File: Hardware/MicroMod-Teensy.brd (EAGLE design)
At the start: 22 x 22.8 mm, 76 parts, among them J1 MICROMOD-2222, Q1 20V/4.2A/52mΩ/1.4W, Q2 20V/0.2A/8MHz/1.2Ω/1Vth, U1 IMXRT1062DV10X10, U2 W25QXX3X2, U3 MKL02Z32VFG4, Y1 32.768kHz, Y2 24MHz

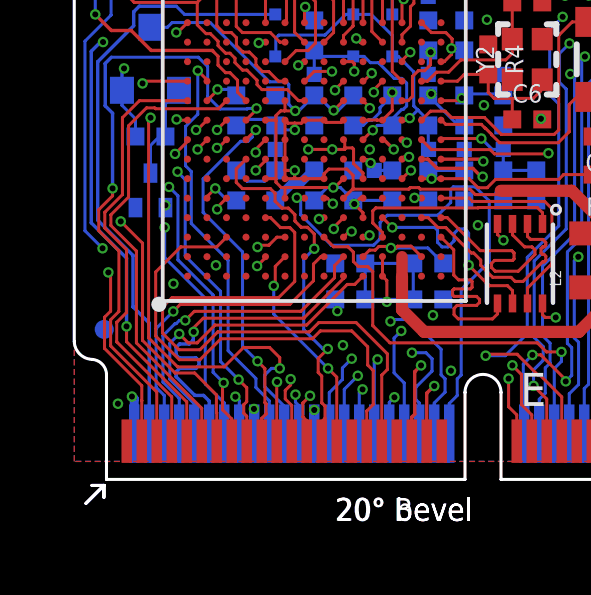
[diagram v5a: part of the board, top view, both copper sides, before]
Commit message: Add ordering instructions
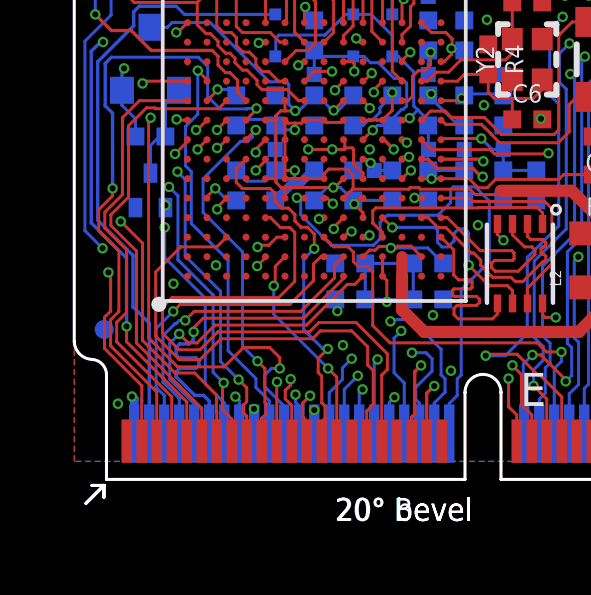
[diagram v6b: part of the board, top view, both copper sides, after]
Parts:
- added LOGO3: SPECIAL_INSTRUCTIONS-ORDERING, SparkFun-Aesthetics:ORDERING_INSTRUCTIONS
- moved LOGO2 24.2 mm to (11.4, -21.6)
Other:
- board text added: "0.8mm PCB 45 degree chamfered edge Four layer design"
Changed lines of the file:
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@@
 <?xml version="1.0" encoding="utf-8"?>
 <!DOCTYPE eagle SYSTEM "eagle.dtd">
-<eagle version="9.5.2">
+<eagle version="9.6.0">
 <drawing>
 <settings>
@@
 <setting verticaltext="up"/>
 </settings>
-<grid distance="1" unitdist="mm" unit="mm" style="lines" multiple="1" display="yes" altdistance="0.05" altunitdist="mm" altunit="mm"/>
+<grid distance="0.05" unitdist="inch" unit="inch" style="lines" multiple="1" display="yes" altdistance="0.005" altunitdist="inch" altunit="inch"/>
 <layers>
 <layer number="1" name="Top" color="4" fill="1" visible="yes" active="yes"/>
-<layer number="2" name="Horz" color="1" fill="3" visible="no" active="yes"/>
-<layer number="15" name="Vert" color="4" fill="6" visible="no" active="yes"/>
+<layer number="2" name="Horz" color="1" fill="3" visible="yes" active="yes"/>
+<layer number="15" name="Vert" color="4" fill="6" visible="yes" active="yes"/>
 <layer number="16" name="Bottom" color="1" fill="1" visible="yes" active="yes"/>
 <layer number="17" name="Pads" color="2" fill="1" visible="yes" active="yes"/>
@@
 <layer number="23" name="tOrigins" color="15" fill="1" visible="yes" active="yes"/>
 <layer number="24" name="bOrigins" color="15" fill="1" visible="yes" active="yes"/>
-<layer number="25" name="tNames" color="7" fill="1" visible="no" active="yes"/>
-<layer number="26" name="bNames" color="7" fill="1" visible="no" active="yes"/>
-<layer number="27" name="tValues" color="7" fill="1" visible="no" active="yes"/>
-<layer number="28" name="bValues" color="7" fill="1" visible="no" active="yes"/>
-<layer number="29" name="tStop" color="7" fill="3" visible="no" active="yes"/>
-<layer number="30" name="bStop" color="7" fill="6" visible="no" active="yes"/>
-<layer number="31" name="tCream" color="7" fill="4" visible="no" active="yes"/>
-<layer number="32" name="bCream" color="7" fill="5" visible="no" active="yes"/>
-<layer number="33" name="tFinish" color="6" fill="3" visible="no" active="yes"/>
-<layer number="34" name="bFinish" color="6" fill="6" visible="no" active="yes"/>
-<layer number="35" name="tGlue" color="7" fill="4" visible="no" active="yes"/>
-<layer number="36" name="bGlue" color="7" fill="5" visible="no" active="yes"/>
-<layer number="37" name="tTest" color="7" fill="1" visible="no" active="yes"/>
-<layer number="38" name="bTest" color="7" fill="1" visible="no" active="yes"/>
-<layer number="39" name="tKeepout" color="4" fill="11" visible="no" active="yes"/>
-<layer number="40" name="bKeepout" color="1" fill="11" visible="no" active="yes"/>
-<layer number="41" name="tRestrict" color="4" fill="10" visible="no" active="yes"/>
-<layer number="42" name="bRestrict" color="1" fill="10" visible="no" active="yes"/>
-<layer number="43" name="vRestrict" color="2" fill="10" visible="no" active="yes"/>
-<layer number="44" name="Drills" color="7" fill="1" visible="no" active="yes"/>
+<layer number="25" name="tNames" color="7" fill="1" visible="yes" active="yes"/>
+<layer number="26" name="bNames" color="7" fill="1" visible="yes" active="yes"/>
+<layer number="27" name="tValues" color="7" fill="1" visible="yes" active="yes"/>
+<layer number="28" name="bValues" color="7" fill="1" visible="yes" active="yes"/>
+<layer number="29" name="tStop" color="7" fill="3" visible="yes" active="yes"/>
+<layer number="30" name="bStop" color="7" fill="6" visible="yes" active="yes"/>
+<layer number="31" name="tCream" color="7" fill="4" visible="yes" active="yes"/>
+<layer number="32" name="bCream" color="7" fill="5" visible="yes" active="yes"/>
+<layer number="33" name="tFinish" color="6" fill="3" visible="yes" active="yes"/>
+<layer number="34" name="bFinish" color="6" fill="6" visible="yes" active="yes"/>
+<layer number="35" name="tGlue" color="7" fill="4" visible="yes" active="yes"/>
+<layer number="36" name="bGlue" color="7" fill="5" visible="yes" active="yes"/>
+<layer number="37" name="tTest" color="7" fill="1" visible="yes" active="yes"/>
+<layer number="38" name="bTest" color="7" fill="1" visible="yes" active="yes"/>
+<layer number="39" name="tKeepout" color="4" fill="11" visible="yes" active="yes"/>
+<layer number="40" name="bKeepout" color="1" fill="11" visible="yes" active="yes"/>
+<layer number="41" name="tRestrict" color="4" fill="10" visible="yes" active="yes"/>
+<layer number="42" name="bRestrict" color="1" fill="10" visible="yes" active="yes"/>
+<layer number="43" name="vRestrict" color="2" fill="10" visible="yes" active="yes"/>
+<layer number="44" name="Drills" color="7" fill="1" visible="yes" active="yes"/>
 <layer number="45" name="Holes" color="7" fill="1" visible="yes" active="yes"/>
-<layer number="46" name="Milling" color="3" fill="1" visible="no" active="yes"/>
-<layer number="47" name="Measures" color="7" fill="1" visible="no" active="yes"/>
-<layer number="48" name="Document" color="7" fill="1" visible="no" active="yes"/>
+<layer number="46" name="Milling" color="3" fill="1" visible="yes" active="yes"/>
+<layer number="47" name="Measures" color="7" fill="1" visible="yes" active="yes"/>
+<layer number="48" name="Document" color="7" fill="1" visible="yes" active="yes"/>
 <layer number="49" name="Reference" color="7" fill="1" visible="yes" active="yes"/>
-<layer number="50" name="dxf" color="7" fill="1" visible="no" active="yes"/>
+<layer number="50" name="dxf" color="7" fill="1" visible="yes" active="yes"/>
 <layer number="51" name="tDocu" color="6" fill="1" visible="yes" active="yes"/>
-<layer number="52" name="bDocu" color="7" fill="1" visible="no" active="yes"/>
+<layer number="52" name="bDocu" color="7" fill="1" visible="yes" active="yes"/>
 <layer number="91" name="Nets" color="2" fill="1" visible="no" active="no"/>
 <layer number="92" name="Busses" color="1" fill="1" visible="no" active="no"/>
@@
 <wire x1="-0.86" y1="19" x2="-0.86" y2="5" width="0.1016" layer="51"/>
 <text x="19.94" y="6" size="0.75" layer="16" font="vector" ratio="20" rot="MR0" align="center">v11</text>
+<text x="29.53" y="31.67" size="1.778" layer="51" font="vector" ratio="15">0.8mm PCB
+45 degree chamfered edge
+Four layer design</text>
 </plain>
 <attributes>
@@
 <attribute name="VALUE" x="1.68" y="11.992" size="0.6096" layer="28" font="vector" ratio="20" rot="MR180" align="top-center"/>
 </element>
-<element name="LOGO2" library="SparkFun-Aesthetics" package="DUMMY" value="OSHW-LOGONO_SILK" x="-12.7" y="-22.86" smashed="yes"/>
+<element name="LOGO2" library="SparkFun-Aesthetics" package="DUMMY" value="OSHW-LOGONO_SILK" x="11.43" y="-21.59" smashed="yes"/>
+<element name="LOGO3" library="SparkFun-Aesthetics" package="ORDERING_INSTRUCTIONS" value="SPECIAL_INSTRUCTIONS-ORDERING" x="26.67" y="50.8" smashed="yes"/>
 </elements>
 <signals>
@@
 <wire x1="1.12125" y1="15.12125" x2="-0.07775" y2="13.92225" width="0.1143" layer="16"/>
 <wire x1="-0.07775" y1="8.6426125" x2="1.0995" y2="7.4653625" width="0.1143" layer="16"/>
-<wire x1="1.0995" y1="5.7505" x2="1.1" y2="5.75" width="0.1143" layer="16"/>
 <wire x1="1.0995" y1="7.4653625" x2="1.0995" y2="5.7505" width="0.1143" layer="16"/>
 <wire x1="1.12125" y1="15.58575625" x2="1.12125" y2="15.12125" width="0.1143" layer="16"/>
 <wire x1="-0.07775" y1="13.92225" x2="-0.07775" y2="8.6426125" width="0.1143" layer="16"/>
 <wire x1="1.64" y1="1.525" x2="1.64" y2="5.21" width="0.1143" layer="16"/>
-<wire x1="1.64" y1="5.21" x2="1.1" y2="5.75" width="0.1143" layer="16"/>
+<wire x1="1.64" y1="5.21" x2="1.0995" y2="5.7505" width="0.1143" layer="16"/>
 </signal>
 <signal name="PROGRAM">
@@
 <wire x1="14.50485" y1="4.82446875" x2="14.50485" y2="9.65433125" width="0.1143" layer="15"/>
 <wire x1="14.50485" y1="9.65433125" x2="13.70485" y2="10.45433125" width="0.1143" layer="15"/>
-<wire x1="13.70485" y1="10.45433125" x2="13.70485" y2="11" width="0.1143" layer="15"/>
-<wire x1="13.70485" y1="11" x2="13.70485" y2="11.25" width="0.1143" layer="15"/>
 <wire x1="11.47074375" y1="19.38495" x2="11.19325625" y2="19.38495" width="0.1143" layer="15"/>
 <wire x1="11.19325625" y1="19.38495" x2="11.18619375" y2="19.3778875" width="0.1143" layer="15"/>
 <wire x1="11.18619375" y1="19.3778875" x2="10.9721125" y2="19.3778875" width="0.1143" layer="15"/>
-<wire x1="13.70485" y1="11.25" x2="13.70485" y2="17.15084375" width="0.1143" layer="15"/>
+<wire x1="13.70485" y1="10.45433125" x2="13.70485" y2="17.15084375" width="0.1143" layer="15"/>
 <wire x1="13.70485" y1="17.15084375" x2="11.47074375" y2="19.38495" width="0.1143" layer="15"/>
 </signal>
@@
 </drawing>
 <compatibility>
+<note version="6.3" minversion="6.2.2" severity="warning">
+Since Version 6.2.2 text objects can contain more than one line,
+which will not be processed correctly with this version.
+</note>
 <note version="8.3" severity="warning">
 Since Version 8.3, EAGLE supports URNs for individual library

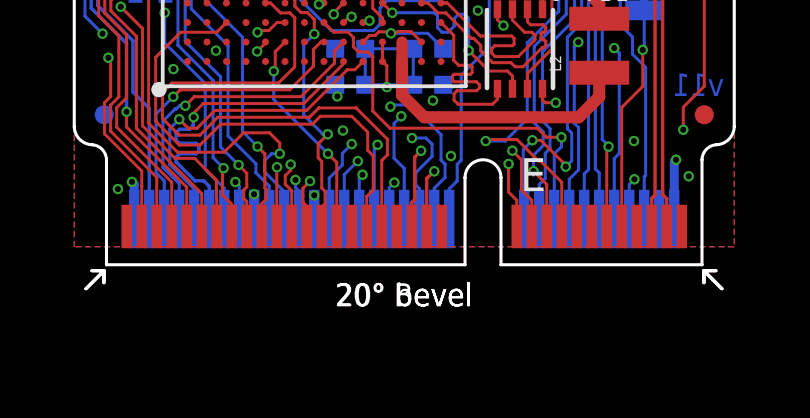
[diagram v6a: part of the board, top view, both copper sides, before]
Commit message: Update Micromod connector to current version
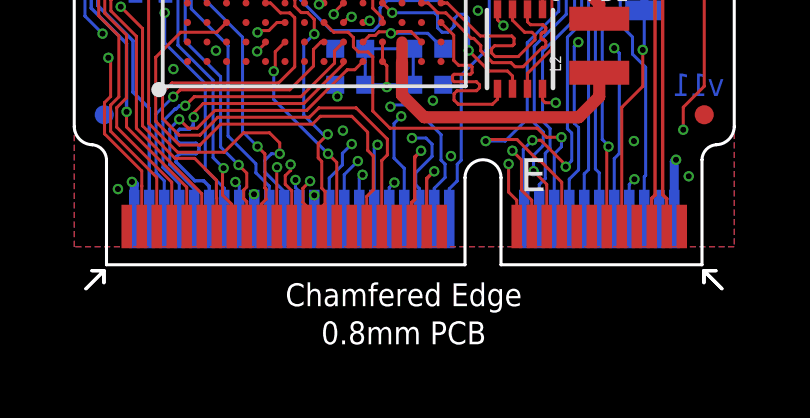
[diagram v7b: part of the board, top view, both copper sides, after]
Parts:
- J1: device Teensy:M.2-CARD-E-22 -> SparkFun-MicroMod:M.2-CARD-E-22
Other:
- board text removed: "20° bevel"
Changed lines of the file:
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@@
 <wire x1="0.215" y1="0" x2="0.215" y2="3.5" width="0.1016" layer="20"/>
 <wire x1="20.065" y1="3.5" x2="20.065" y2="0" width="0.1016" layer="20"/>
-<text x="10.14" y="-1" size="0.762" layer="46" rot="R180" align="center">20° bevel</text>
 <wire x1="20.54" y1="4" x2="20.065" y2="3.5" width="0.1016" layer="20" curve="84.949116"/>
 <wire x1="-0.26" y1="4" x2="0.215" y2="3.5" width="0.1016" layer="20" curve="-83.820277"/>
@@
 <element name="U$5" library="buzzard_labels (1)" package="MICROMOD0" value="" x="20.74" y="15.5" smashed="yes" rot="MR0"/>
 <element name="U$7" library="SparkFun-Buzzard" package="MEAS_32" value="" x="20.24" y="6.6" smashed="yes" rot="MR90"/>
-<element name="J1" library="Teensy" package="M.2-CARD-E-22" value="MICROMOD-2222" x="10.14" y="0" smashed="yes"/>
+<element name="J1" library="SparkFun-MicroMod" package="M.2-CARD-E-22" value="MICROMOD-2222" x="10.14" y="0" smashed="yes"/>
 <element name="TP2" library="SparkFun-Connectors" package="PAD.02X.02" value="" x="9.14" y="10.3" smashed="yes" rot="MR0"/>
 <element name="Q1" library="SparkFun-DiscreteSemi" package="SOT23-3" value="20V/4.2A/52mΩ/1.4W" x="1.68" y="13.97" smashed="yes" rot="MR0">
@@
 <wire x1="7.0984" y1="10.3" x2="7.14" y2="10.3" width="0.3048" layer="16"/>
 <wire x1="6.6682" y1="9.8698" x2="7.0984" y2="10.3" width="0.3048" layer="16"/>
+<wire x1="14.14" y1="22" x2="18.263" y2="21" width="0" layer="19" extent="1-1"/>
+<wire x1="14.14" y1="19" x2="14.14" y2="22" width="0" layer="19" extent="16-16"/>
+<wire x1="14.74" y1="15.9" x2="14.14" y2="18.17145" width="0" layer="19" extent="1-16"/>
+<wire x1="15.496" y1="16.123" x2="14.74" y2="15.9" width="0" layer="19" extent="1-1"/>
+<wire x1="12.896" y1="15.323" x2="14.74" y2="15.9" width="0" layer="19" extent="1-1"/>
+<wire x1="12.14" y1="15.3" x2="12.896" y2="15.323" width="0" layer="19" extent="16-16"/>
+<wire x1="11.365" y1="15.225" x2="12.14" y2="15.3" width="0" layer="19" extent="1-16"/>
+<wire x1="10.94" y1="15.3" x2="11.365" y2="15.225" width="0" layer="19" extent="1-16"/>
+<wire x1="12.94" y1="14.5" x2="12.896" y2="15.323" width="0" layer="19" extent="1-1"/>
+<wire x1="12.196" y1="16.223" x2="12.14" y2="15.3" width="0" layer="19" extent="16-16"/>
+<wire x1="12.796" y1="12.473" x2="12.94" y2="14.5" width="0" layer="19" extent="1-1"/>
+<wire x1="13.44" y1="11.8" x2="12.796" y2="12.473" width="0" layer="19" extent="16-16"/>
+<wire x1="12.14" y1="11.8" x2="12.796" y2="12.473" width="0" layer="19" extent="16-16"/>
+<wire x1="11.04" y1="12.85" x2="10.94" y2="12.8" width="0" layer="19" extent="16-16"/>
+<wire x1="9.74" y1="12.8" x2="9.74" y2="12.9" width="0" layer="19" extent="16-16"/>
+<wire x1="8.115" y1="11.325" x2="8.44" y2="11.8" width="0" layer="19" extent="1-16"/>
+<wire x1="6.815" y1="11.325" x2="6.94" y2="11" width="0" layer="19" extent="1-1"/>
+<wire x1="6.815" y1="10.675" x2="6.94" y2="11" width="0" layer="19" extent="1-1"/>
+<wire x1="6.9547125" y1="10.3" x2="6.815" y2="10.675" width="0" layer="19" extent="1-16"/>
+<wire x1="8.44" y1="10.3" x2="8.765" y2="10.025" width="0" layer="19" extent="1-16"/>
+<wire x1="7.465" y1="10.675" x2="7.74" y2="11" width="0" layer="19" extent="1-1"/>
+<wire x1="7.465" y1="11.325" x2="7.74" y2="11" width="0" layer="19" extent="1-1"/>
+<wire x1="8.115" y1="10.675" x2="7.74" y2="11" width="0" layer="19" extent="1-1"/>
+<wire x1="7.14" y1="11.8" x2="6.815" y2="11.325" width="0" layer="19" extent="1-16"/>
+<wire x1="8.99" y1="11" x2="8.44" y2="10.3" width="0" layer="19" extent="16-16"/>
+<wire x1="14.696" y1="12.023" x2="13.44" y2="11.8" width="0" layer="19" extent="16-16"/>
+<wire x1="14.74" y1="12" x2="14.696" y2="12.023" width="0" layer="19" extent="1-1"/>
+<wire x1="14.946" y1="10.873" x2="14.74" y2="12" width="0" layer="19" extent="1-1"/>
+<wire x1="4.54" y1="9.3" x2="5.84" y2="9.3" width="0" layer="19" extent="16-16"/>
+<wire x1="16.42" y1="11.43" x2="14.946" y2="10.873" width="0" layer="19" extent="1-1"/>
+<wire x1="17.14" y1="10.8" x2="16.42" y2="11.43" width="0" layer="19" extent="1-1"/>
+<wire x1="17.99" y1="11.9" x2="17.14" y2="10.8" width="0" layer="19" extent="1-1"/>
+<wire x1="18.14" y1="13.5" x2="17.99" y2="11.9" width="0" layer="19" extent="1-1"/>
+<wire x1="18.846" y1="14.023" x2="18.14" y2="13.5" width="0" layer="19" extent="1-1"/>
+<wire x1="18.14" y1="14.5" x2="18.846" y2="14.023" width="0" layer="19" extent="1-1"/>
+<wire x1="14.54" y1="9.3" x2="14.946" y2="10.873" width="0" layer="19" extent="16-16"/>
+<wire x1="13.44" y1="9.3" x2="14.54" y2="9.3" width="0" layer="19" extent="16-16"/>
+<wire x1="13.248" y1="8.515" x2="13.44" y2="9.3" width="0" layer="19" extent="1-16"/>
+<wire x1="12.596" y1="8.473" x2="13.248" y2="8.515" width="0" layer="19" extent="1-1"/>
+<wire x1="12.14" y1="9.3" x2="12.596" y2="8.473" width="0" layer="19" extent="16-16"/>
+<wire x1="10.94" y1="9.3" x2="12.14" y2="9.3" width="0" layer="19" extent="16-16"/>
+<wire x1="10.715" y1="9.375" x2="10.94" y2="9.3" width="0" layer="19" extent="1-16"/>
+<wire x1="5.84" y1="12.8" x2="7.14" y2="11.8" width="0" layer="19" extent="16-16"/>
+<wire x1="4.54" y1="12.8" x2="5.84" y2="12.8" width="0" layer="19" extent="16-16"/>
+<wire x1="11.44" y1="7.2" x2="12.596" y2="8.473" width="0" layer="19" extent="16-16"/>
+<wire x1="11.365" y1="6.775" x2="11.44" y2="7.2" width="0" layer="19" extent="1-16"/>
+<wire x1="10.715" y1="6.775" x2="10.715" y2="7.425" width="0" layer="19" extent="1-1"/>
+<wire x1="11.44" y1="6" x2="11.365" y2="6.775" width="0" layer="19" extent="1-16"/>
+<wire x1="11.096" y1="5.473" x2="11.44" y2="6" width="0" layer="19" extent="16-16"/>
+<wire x1="7.84" y1="7.2" x2="8.765" y2="7.425" width="0" layer="19" extent="1-16"/>
+<wire x1="10.396" y1="4.223" x2="11.096" y2="5.473" width="0" layer="19" extent="1-1"/>
+<wire x1="11.39" y1="1.275" x2="10.64" y2="1.525" width="0" layer="19" extent="1-16"/>
+<wire x1="9.89" y1="1.275" x2="10.64" y2="1.525" width="0" layer="19" extent="1-16"/>
+<wire x1="11.696" y1="3.623" x2="10.396" y2="4.223" width="0" layer="19" extent="1-1"/>
+<wire x1="8.39" y1="1.275" x2="9.89" y2="1.275" width="0" layer="19" extent="1-1"/>
+<wire x1="20.546" y1="14.623" x2="18.846" y2="14.023" width="0" layer="19" extent="1-1"/>
+<wire x1="5.515" y1="14.575" x2="5.84" y2="12.8" width="0" layer="19" extent="1-16"/>
+<wire x1="6.815" y1="15.225" x2="5.515" y2="14.575" width="0" layer="19" extent="1-1"/>
+<wire x1="8.54" y1="14.7" x2="7.14" y2="15.3" width="0" layer="19" extent="16-16"/>
+<wire x1="5.515" y1="7.425" x2="5.84" y2="9.3" width="0" layer="19" extent="1-16"/>
+<wire x1="8.096" y1="4.473" x2="10.396" y2="4.223" width="0" layer="19" extent="1-1"/>
+<wire x1="2.54" y1="14.9" x2="3.91551875" y2="13" width="0" layer="19" extent="1-1"/>
+<wire x1="2.74" y1="16.6" x2="2.915" y2="15.225" width="0" layer="19" extent="1-1"/>
+<wire x1="2.89" y1="17.5" x2="2.74" y2="16.6" width="0" layer="19" extent="1-1"/>
+<wire x1="3.14" y1="19" x2="2.89" y2="17.5" width="0" layer="19" extent="1-1"/>
+<wire x1="2.915" y1="6.775" x2="5.236" y2="7.112" width="0" layer="19" extent="1-1"/>
+<wire x1="2.446" y1="6.523" x2="2.915" y2="6.775" width="0" layer="19" extent="1-1"/>
+<wire x1="1.18" y1="9.06" x2="3.565" y2="9.375" width="0" layer="19" extent="1-16"/>
+<wire x1="0.14" y1="18.5" x2="2.89" y2="17.5" width="0" layer="19" extent="1-1"/>
+<wire x1="-0.46" y1="19" x2="0.14" y2="18.5" width="0" layer="19" extent="1-1"/>
+<wire x1="0.14" y1="20.5" x2="-0.46" y2="19" width="0" layer="19" extent="1-1"/>
+<wire x1="-0.26" y1="21.2" x2="0.14" y2="20.5" width="0" layer="19" extent="1-1"/>
+<wire x1="0.596" y1="2.523" x2="2.446" y2="6.523" width="0" layer="19" extent="1-1"/>
+<wire x1="0.89" y1="1.275" x2="0.596" y2="2.523" width="0" layer="19" extent="1-1"/>
+<wire x1="17.796" y1="4.123" x2="13.446" y2="7.973" width="0" layer="19" extent="1-1"/>
+<wire x1="19.623" y1="2.95" x2="17.796" y2="4.123" width="0" layer="19" extent="1-1"/>
+<wire x1="19.39" y1="1.275" x2="19.623" y2="2.95" width="0" layer="19" extent="1-1"/>
+<wire x1="17.89" y1="1.275" x2="19.39" y2="1.275" width="0" layer="19" extent="1-1"/>
 </signal>
 <signal name="3.3V">
@@
 <wire x1="0.73" y1="12.97" x2="0.73" y2="13.63" width="0.1143" layer="16"/>
 <wire x1="0.73" y1="13.63" x2="0.8" y2="13.7" width="0.1143" layer="16"/>
+<wire x1="2.39" y1="17.5" x2="5.44" y2="21" width="0" layer="19" extent="1-1"/>
+<wire x1="0.14" y1="19.5" x2="2.39" y2="17.5" width="0" layer="19" extent="1-1"/>
+<wire x1="0.8" y1="13.7" x2="2.24" y2="16.6" width="0" layer="19" extent="1-1"/>
+<wire x1="9.77535" y1="17.6731" x2="6.263" y2="21" width="0" layer="19" extent="1-1"/>
+<wire x1="7.84" y1="6" x2="1.18" y2="11.43" width="0" layer="19" extent="16-16"/>
+<wire x1="14.748" y1="5.865" x2="7.909815625" y2="5.610184375" width="0" layer="19" extent="1-1"/>
+<wire x1="19.2" y1="3.5" x2="15.19" y2="5.4" width="0" layer="19" extent="1-1"/>
+<wire x1="1.06264375" y1="2.76264375" x2="7.909815625" y2="5.610184375" width="0" layer="19" extent="1-1"/>
 </signal>
 <signal name="USB_D+" class="1">
